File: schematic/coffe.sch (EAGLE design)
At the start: 16 parts, among them Q1 BC546B

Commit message: New Updated schematic, need some fix
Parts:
- WATER: value (none) -> Water
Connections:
- new net N$8: BOARD1.3V3, BUTTONADD-2.KL
- net VCC: no longer BUTTONADD-2.KL
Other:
- moved on the sheet: RELE, WATER

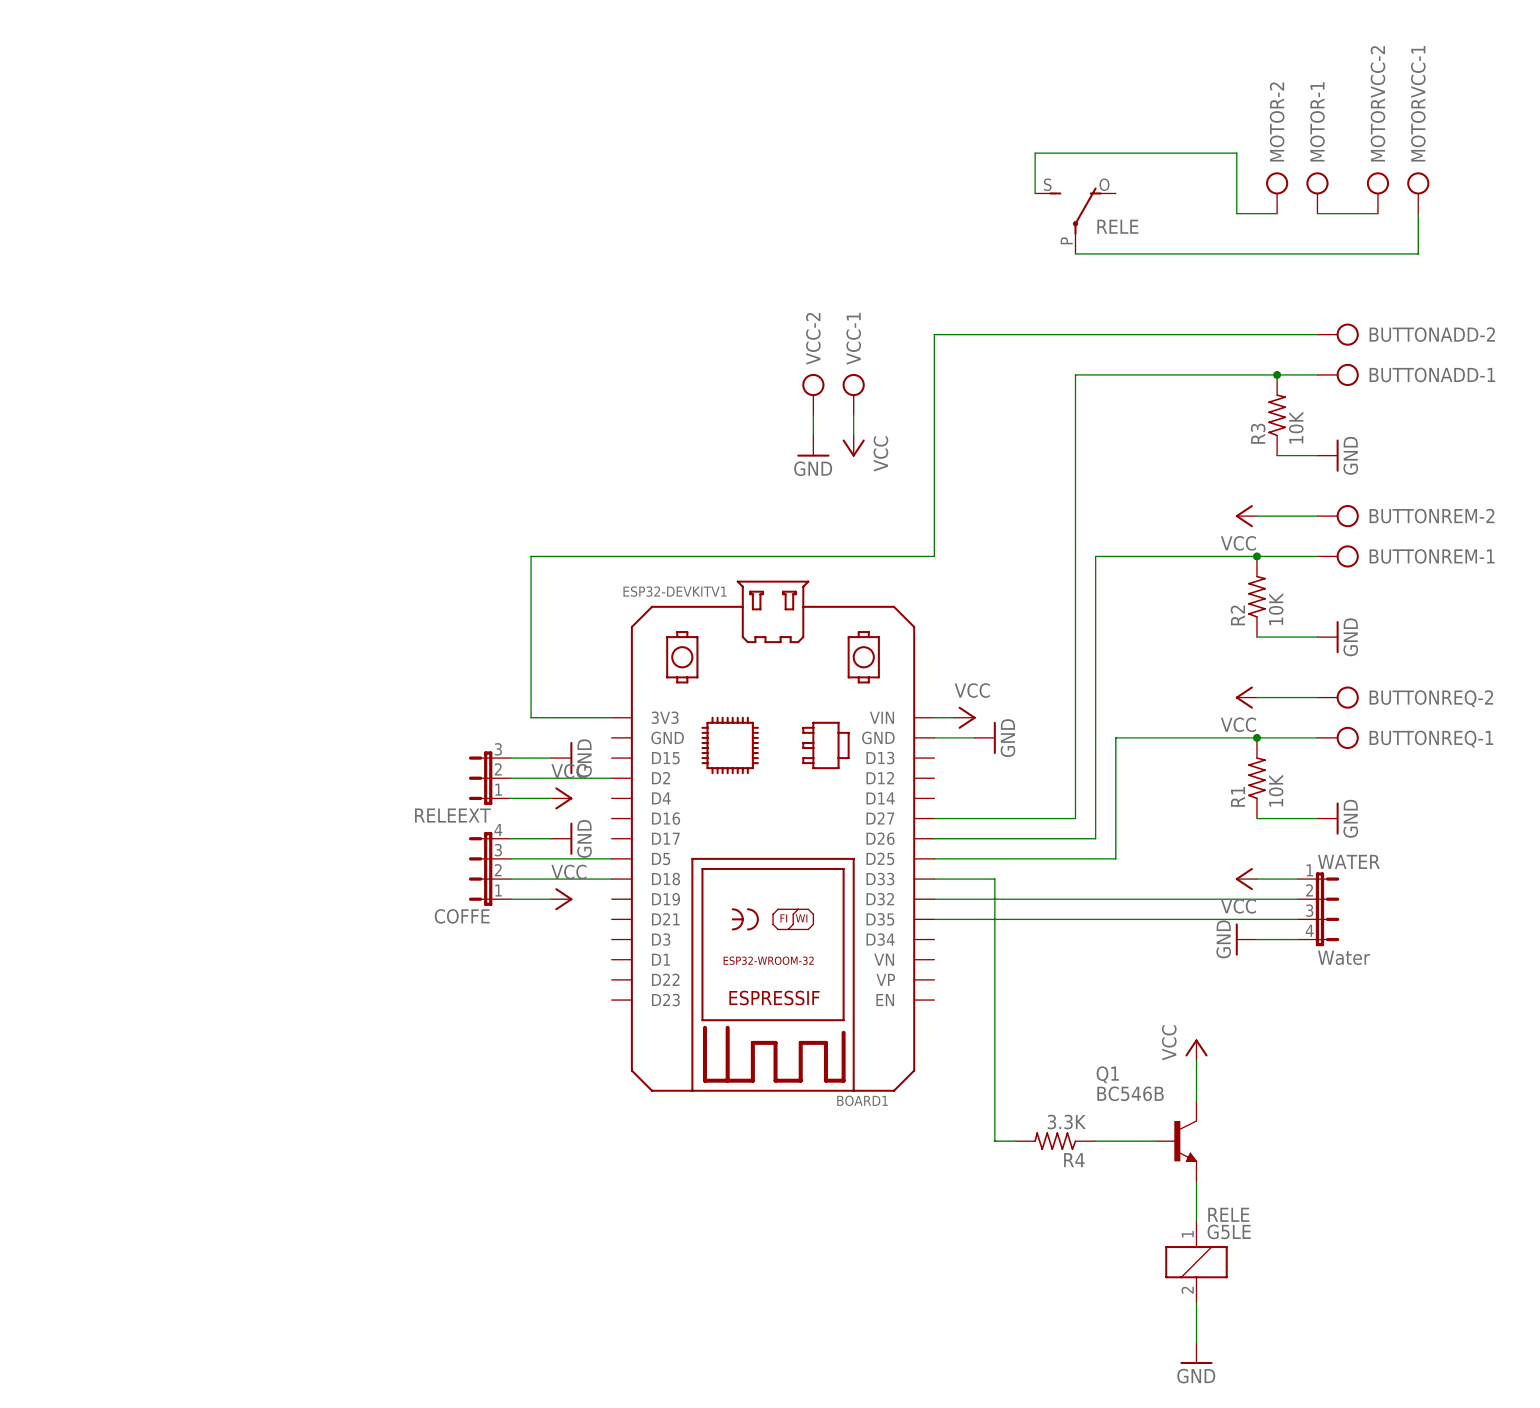
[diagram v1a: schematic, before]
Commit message: New schematic design, should make it better
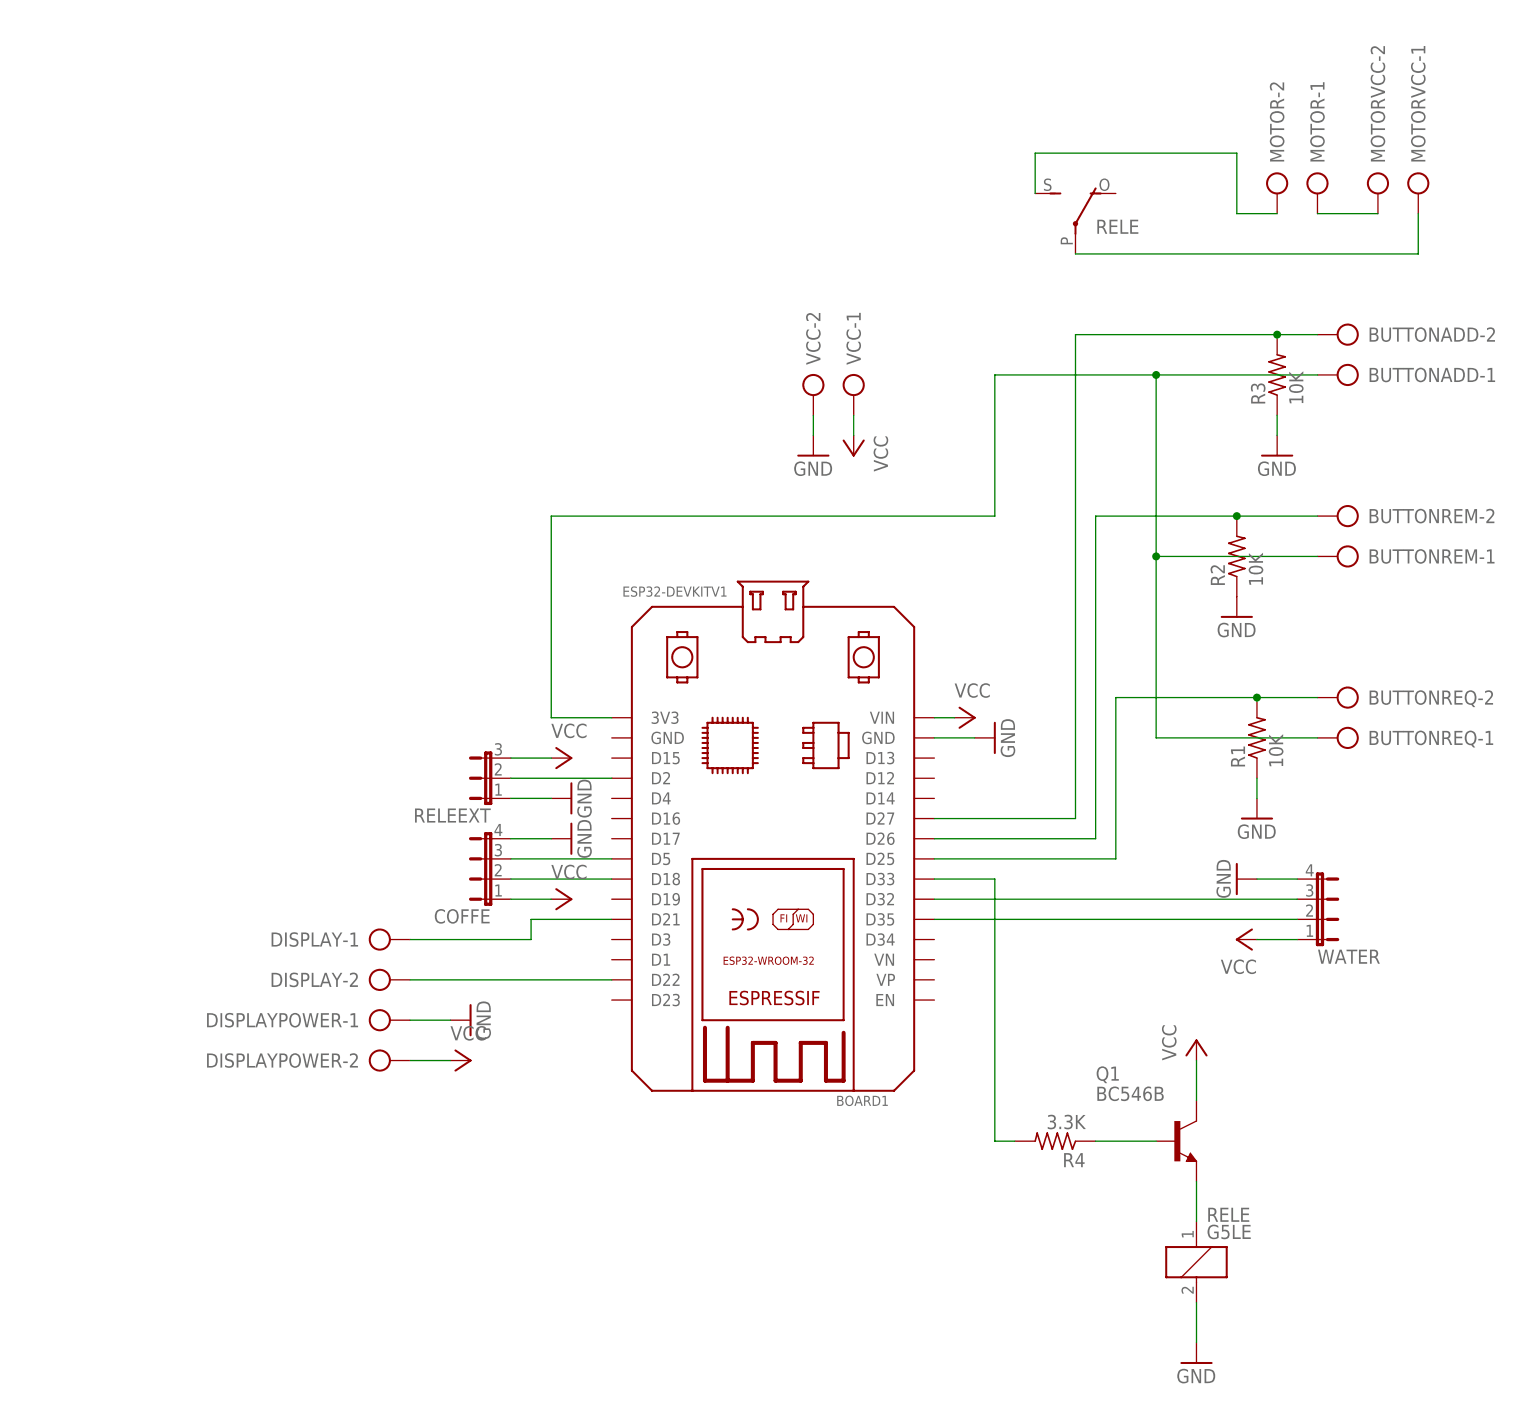
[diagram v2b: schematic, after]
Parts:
- added DISPLAY, DISPLAYPOWER: (no value), con-ptr500:AK500/2-H
- WATER: value Water -> (none)
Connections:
- removed net N$5: BOARD1.D26, BUTTONREM-1.KL, R2.2
- new net N$16: BOARD1.D27, BUTTONADD-2.KL, R3.2
- new net N$17: BOARD1.D21, DISPLAY-1.KL
- new net N$18: BOARD1.D26, BUTTONREM-2.KL, R2.2
- net GND: now also DISPLAYPOWER-1.KL, RELEEXT.1; no longer RELEEXT.3
- net N$1: now also WATER.3; no longer WATER.2
- net N$15: now also BOARD1.3V3, BUTTONADD-1.KL, BUTTONREM-1.KL; no longer BOARD1.D25, R1.2
- net N$2: now also WATER.2; no longer WATER.3
- net N$6: now also BOARD1.D25, BUTTONREQ-2.KL, R1.2; no longer BOARD1.D27, BUTTONADD-1.KL, R3.2
- net N$8: now also BOARD1.D22, DISPLAY-2.KL; no longer BOARD1.3V3, BUTTONADD-2.KL
- net VCC: now also DISPLAYPOWER-2.KL, RELEEXT.3; no longer BUTTONREM-2.KL, BUTTONREQ-2.KL, RELEEXT.1
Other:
- moved on the sheet: R1, R2, R3, WATER

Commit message: Routing complete
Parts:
- removed R1, R2, R3: 10K, rcl:R-US_0204/7
- added PADGND, PADGND1, PADGND2, VINSHORT, VINSHORT1: (no value), wirepad:2,15/1,0
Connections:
- removed net N$7 (its old number): BOARD1.D33, R4.2
- new net N$5: BOARD1.D14, BUTTONREQ-2.KL
- net GND: now also BOARD1.GND@1, PADGND.P, PADGND1.P, PADGND2.P; no longer R1.1, R2.1, R3.1
- net N$1: now also BOARD1.D3; no longer BOARD1.D32
- net N$16: now also BOARD1.D13; no longer BOARD1.D27, R3.2
- net N$18: now also BOARD1.D12; no longer BOARD1.D26, R2.2
- net N$2: now also BOARD1.D1; no longer BOARD1.D35
- net N$6: now also BOARD1.D19, R4.2; no longer BOARD1.D25, BUTTONREQ-2.KL, R1.2
- net VCC: now also VINSHORT.P, VINSHORT1.P
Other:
- moved on the sheet: BUTTONADD-1, BUTTONADD-2, BUTTONREM-1, BUTTONREM-2, BUTTONREQ-1, BUTTONREQ-2, COFFE, DISPLAY-1, DISPLAY-2, DISPLAYPOWER-1, DISPLAYPOWER-2, MOTOR-1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
